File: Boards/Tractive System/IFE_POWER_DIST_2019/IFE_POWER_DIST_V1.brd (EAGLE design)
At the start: 71.1 x 100 mm, 27 parts, among them X1 5566-8, X2 5566-6

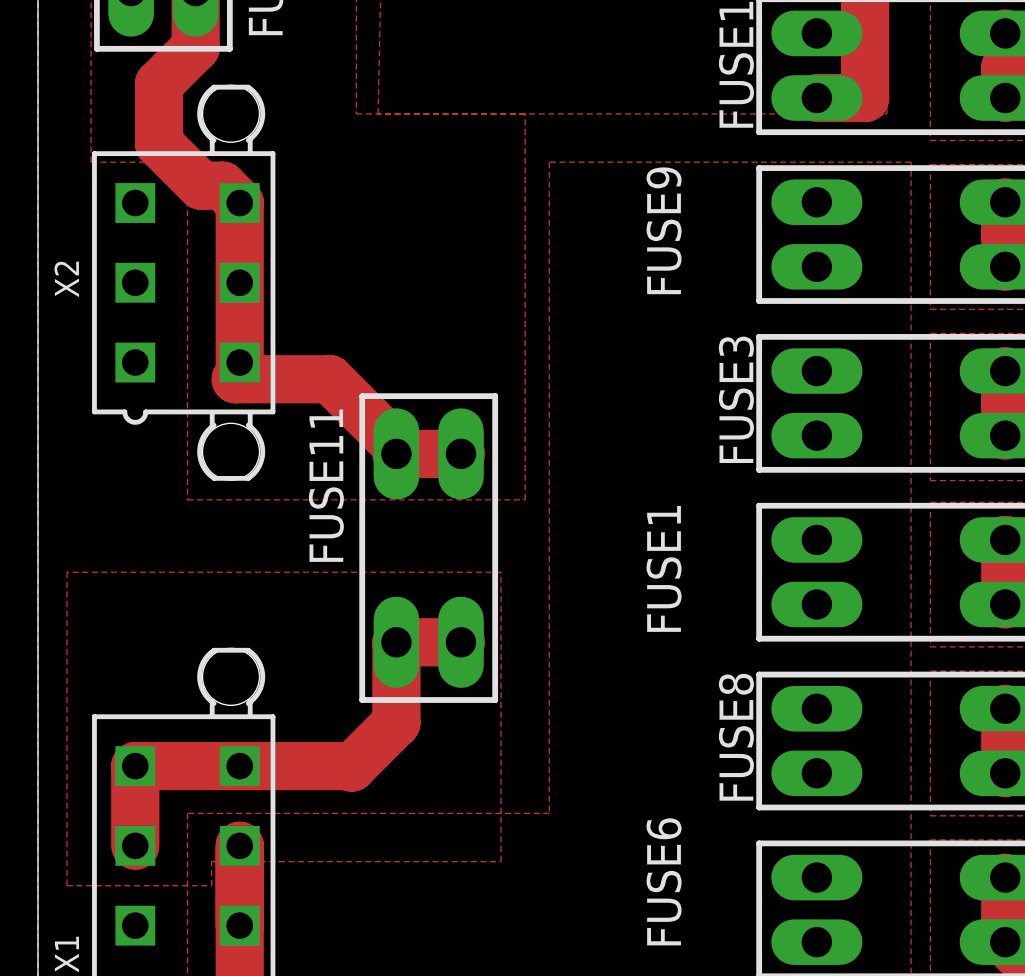
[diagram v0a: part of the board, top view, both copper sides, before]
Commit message: fuse replacement
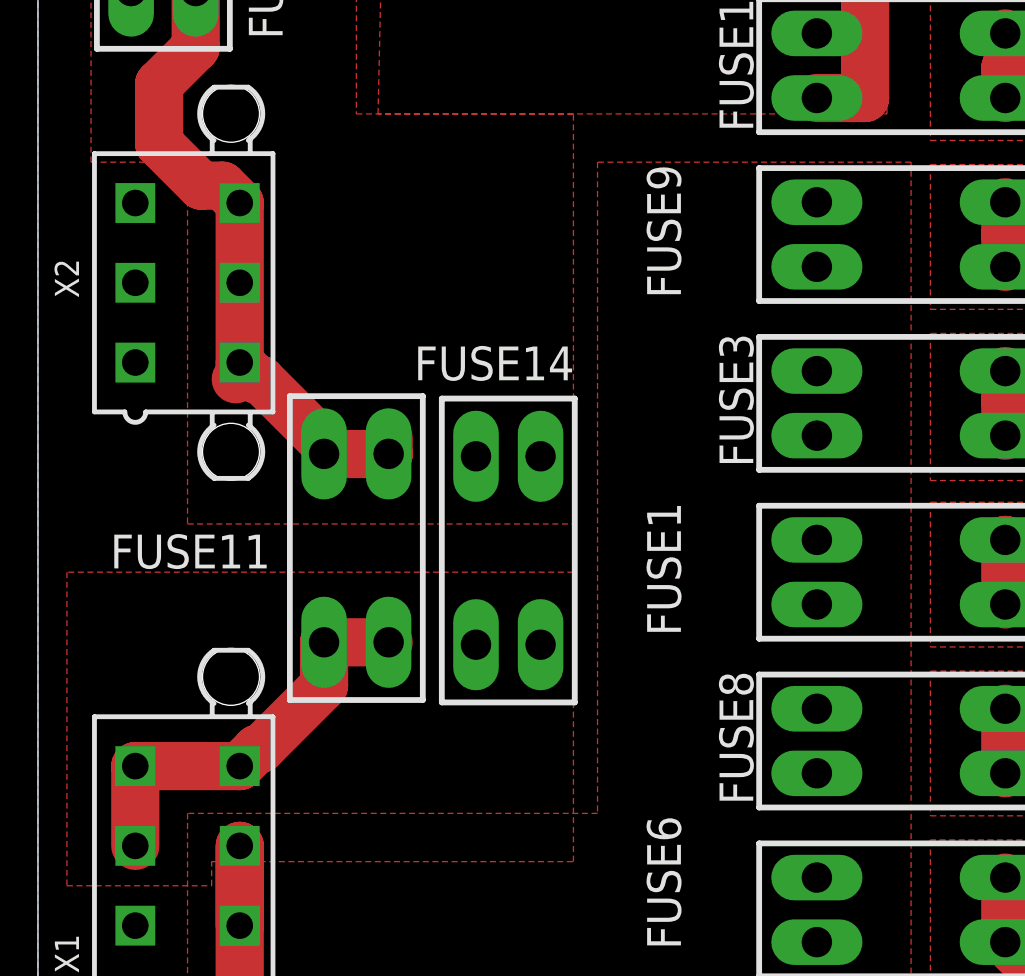
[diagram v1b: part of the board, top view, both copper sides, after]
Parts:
- added FUSE14: V_BAT_12V, Fuse:3568
- moved FUSE11 3.81 mm to (16.8, 34.4)
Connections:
- net VCC: now also FUSE14.P$1, FUSE14.P$4
- net V_BAT_12V: now also FUSE14.P$2, FUSE14.P$3
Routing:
- net V_BAT_12V: track 26.6 -> 21.6 mm
- net VCC: track 37.6 -> 34.6 mm
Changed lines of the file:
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@@
 <attribute name="NAME" x="37.664" y="10.167" size="1.778" layer="21" rot="R270" align="top-left"/>
 </element>
-<element name="FUSE11" library="Fuse" package="3568" value="V_BAT_12V" x="20.574" y="34.417" smashed="yes" rot="R270">
-<attribute name="NAME" x="16.074" y="41.917" size="1.778" layer="21" rot="R270" align="top-left"/>
+<element name="FUSE11" library="Fuse" package="3568" value="V_BAT_12V" x="16.764" y="34.417" smashed="yes" rot="R270">
+<attribute name="NAME" x="3.803" y="35.124" size="1.778" layer="21" align="top-left"/>
 </element>
 <element name="FUSE12" library="Fuse" package="3568" value="V_BAT_5V" x="6.604" y="68.707" smashed="yes" rot="R90">
@@
 <element name="U$6" library="Display_Custom" package="MINIFIT_JR_5566-02" value="MINIFIT_JR_5566-02" x="61.214" y="59.817" smashed="yes" rot="R90">
 <attribute name="NAME" x="67.3926" y="56.9198" size="0.8128" layer="25" rot="R180"/>
+</element>
+<element name="FUSE14" library="Fuse" package="3568" value="V_BAT_12V" x="24.765" y="34.29" smashed="yes" rot="R270">
+<attribute name="NAME" x="19.805" y="45.03" size="1.778" layer="21" align="top-left"/>
 </element>
 </elements>
@@
 <wire x1="10.624" y1="52.587" x2="10.624" y2="43.517" width="2.54" layer="1"/>
 <wire x1="10.624" y1="43.517" x2="10.414" y2="43.307" width="2.54" layer="1"/>
-<wire x1="10.414" y1="43.307" x2="15.367" y2="43.307" width="2.54" layer="1"/>
-<wire x1="18.874" y1="39.8" x2="18.874" y2="39.377" width="2.54" layer="1"/>
-<wire x1="15.367" y1="43.307" x2="18.874" y2="39.8" width="2.54" layer="1"/>
-<wire x1="22.274" y1="39.377" x2="19.424" y2="39.377" width="2.54" layer="1"/>
-<wire x1="19.001" y1="39.8" x2="18.874" y2="39.8" width="2.54" layer="1"/>
-<wire x1="19.424" y1="39.377" x2="19.001" y2="39.8" width="2.54" layer="1"/>
+<wire x1="18.464" y1="39.377" x2="18.464" y2="40.21" width="2.54" layer="1"/>
 <polygon width="0.4064" layer="1" isolate="0.3048" rank="2">
 <vertex x="18.102384375" y="66.167"/>
@@
 <vertex x="2.794" y="54.737"/>
 <vertex x="7.874" y="54.737"/>
-<vertex x="7.874" y="36.957"/>
-<vertex x="25.654" y="36.957"/>
-<vertex x="25.654" y="57.277"/>
+<vertex x="7.874" y="35.687"/>
+<vertex x="28.194" y="35.687"/>
+<vertex x="28.194" y="57.277"/>
 <vertex x="17.907" y="57.277"/>
 </polygon>
+<contactref element="FUSE14" pad="P$1"/>
+<contactref element="FUSE14" pad="P$4"/>
+<wire x1="10.624" y1="44.187" x2="11.538" y2="43.273" width="2.54" layer="1"/>
+<wire x1="11.538" y1="43.273" x2="11.73221875" y2="43.273" width="2.54" layer="1"/>
+<wire x1="11.73221875" y1="43.273" x2="15.24" y2="39.76521875" width="2.54" layer="1"/>
+<wire x1="15.24" y1="39.76521875" x2="15.24" y2="39.37" width="2.54" layer="1"/>
+<wire x1="15.24" y1="39.37" x2="18.457" y2="39.37" width="2.54" layer="1"/>
+<wire x1="18.457" y1="39.37" x2="18.464" y2="39.377" width="2.54" layer="1"/>
 </signal>
 <signal name="N$2">
@@
 <polygon width="0.4064" layer="1">
 <vertex x="45.974" y="54.737"/>
-<vertex x="26.924" y="54.737"/>
-<vertex x="26.924" y="20.447"/>
+<vertex x="29.464" y="54.737"/>
+<vertex x="29.464" y="20.447"/>
 <vertex x="7.874" y="20.447"/>
 <vertex x="7.874" y="1.397"/>
@@
 <contactref element="FUSE11" pad="P$2"/>
 <contactref element="FUSE11" pad="P$3"/>
-<wire x1="22.274" y1="29.457" x2="18.874" y2="29.457" width="2.54" layer="1"/>
+<wire x1="18.464" y1="29.457" x2="15.064" y2="29.457" width="2.54" layer="1"/>
 <contactref element="X1" pad="8"/>
 <contactref element="X1" pad="3"/>
@@
 <wire x1="10.624" y1="22.937" x2="5.124" y2="22.937" width="2.54" layer="1"/>
 <wire x1="5.124" y1="18.737" x2="5.124" y2="22.937" width="2.54" layer="1"/>
-<wire x1="10.624" y1="22.937" x2="16.433" y2="22.937" width="2.54" layer="1"/>
-<wire x1="16.433" y1="22.937" x2="16.51" y2="22.86" width="2.54" layer="1"/>
-<wire x1="16.51" y1="22.86" x2="18.874" y2="25.224" width="2.54" layer="1"/>
-<wire x1="18.874" y1="25.224" x2="18.874" y2="29.457" width="2.54" layer="1"/>
 <polygon width="0.4064" layer="1" isolate="0.3048" rank="2">
 <vertex x="9.144" y="16.637"/>
 <vertex x="9.144" y="17.907"/>
-<vertex x="24.384" y="17.907"/>
-<vertex x="24.384" y="33.147"/>
+<vertex x="28.194" y="17.907"/>
+<vertex x="28.194" y="33.147"/>
 <vertex x="1.524" y="33.147"/>
 <vertex x="1.524" y="16.637"/>
 </polygon>
+<contactref element="FUSE14" pad="P$2"/>
+<contactref element="FUSE14" pad="P$3"/>
+<wire x1="10.624" y1="22.937" x2="11.538" y2="23.851" width="2.54" layer="1"/>
+<wire x1="11.538" y1="23.851" x2="11.73221875" y2="23.851" width="2.54" layer="1"/>
+<wire x1="11.73221875" y1="23.851" x2="15.064" y2="27.18278125" width="2.54" layer="1"/>
+<wire x1="15.064" y1="27.18278125" x2="15.064" y2="29.457" width="2.54" layer="1"/>
 </signal>
 <signal name="V_BAT_5V">
